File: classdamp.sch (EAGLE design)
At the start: 40 parts, among them IC1 78L05, Q1 BS170, Q10 IRF 9Z34N, Q2 BS170, Q7 IRF 530N, Q8 IRF 530N, Q9 IRF 9Z34N

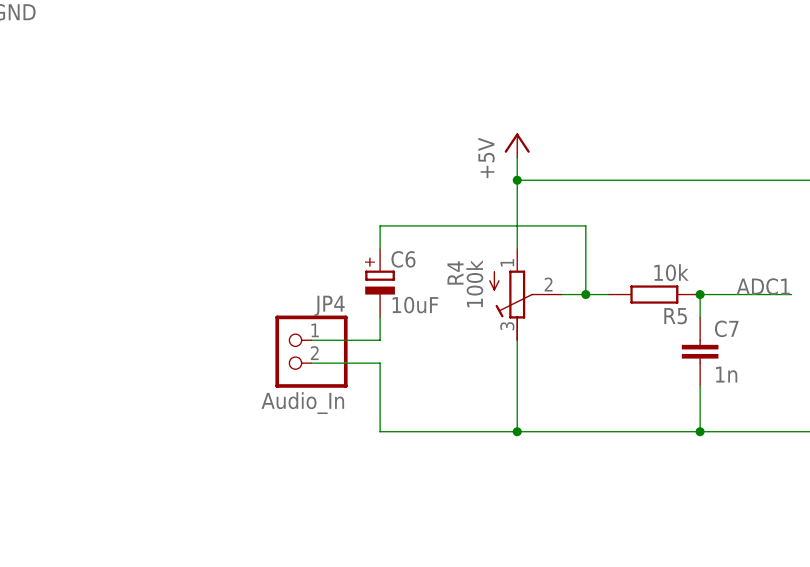
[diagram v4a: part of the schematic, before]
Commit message: updated reichelt order
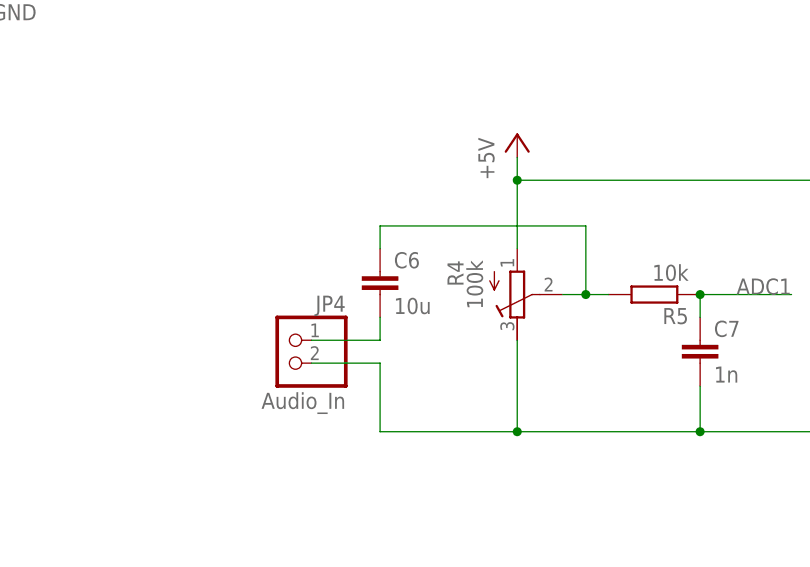
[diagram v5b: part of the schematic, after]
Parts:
- C6: value 10uF -> 10u; device resistor:CPOL-EUE1.8-4 -> resistor:C-EUC0805K
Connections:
- net N$10: now also C6.1; no longer C6.+
- net N$8: now also C6.2; no longer C6.-
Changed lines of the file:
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@@
 <part name="JP6" library="pinhead" deviceset="PINHD-1X3" device="" value="freq_pot"/>
 <part name="JP7" library="pinhead" deviceset="PINHD-1X3" device="" value="vol_pot"/>
-<part name="C6" library="resistor" deviceset="CPOL-EU" device="E1.8-4" value="10uF"/>
 <part name="U$1" library="avr-7" deviceset="TINY26" device="P"/>
 <part name="Q7" library="transistor-power" deviceset="PMOSFET_N" device="TO220BV" value="IRF 530N"/>
@@
 <part name="C7" library="resistor" deviceset="C-EU" device="C0805K" value="1n"/>
 <part name="R5" library="resistor" deviceset="R-EU_" device="R0805" value="10k"/>
+<part name="C6" library="resistor" deviceset="C-EU" device="C0805K" value="10u"/>
 </parts>
 <sheets>
@@
 <instance part="JP6" gate="A" x="91.44" y="0" rot="MR0"/>
 <instance part="JP7" gate="A" x="142.24" y="0" rot="MR0"/>
-<instance part="C6" gate="G$1" x="17.78" y="2.54"/>
 <instance part="U$1" gate="G$1" x="0" y="-60.96"/>
 <instance part="Q7" gate="G$1" x="127" y="45.72"/>
@@
 <instance part="C7" gate="G$1" x="53.34" y="-5.08"/>
 <instance part="R5" gate="G$1" x="48.26" y="0" rot="R180"/>
+<instance part="C6" gate="G$1" x="17.78" y="2.54"/>
 </instances>
 <busses>
@@
 <wire x1="10.16" y1="-5.08" x2="17.78" y2="-5.08" width="0.1524" layer="91"/>
 <wire x1="17.78" y1="-5.08" x2="17.78" y2="-2.54" width="0.1524" layer="91"/>
-<pinref part="C6" gate="G$1" pin="-"/>
+<pinref part="C6" gate="G$1" pin="2"/>
 </segment>
 </net>
 <net name="N$10" class="0">
 <segment>
-<pinref part="C6" gate="G$1" pin="+"/>
 <wire x1="17.78" y1="5.08" x2="17.78" y2="7.62" width="0.1524" layer="91"/>
 <wire x1="17.78" y1="7.62" x2="40.64" y2="7.62" width="0.1524" layer="91"/>
@@
 <junction x="40.64" y="0"/>
 <pinref part="R5" gate="G$1" pin="2"/>
-</segment>
-</net>
+<pinref part="C6" gate="G$1" pin="1"/>
+</segment>
+</net>

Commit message: changed to dual-layer design
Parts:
- added LED2: (no value), led:LEDSML0805
- added R6: 1k, resistor:R-EU_R0805
- D1, D2: device diode:ZENER-DIODEZD-12.5 -> diode:ZENER-DIODEZD-5
- LED1: device led:LED5MM -> led:LEDSML0805
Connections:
- new net N$14: R6.2, U$1.(ADC7/XTAL1)PB4
- new net N$3: LED2.A, R6.1
- net GND: now also LED2.C
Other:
- moved on the sheet: JP8
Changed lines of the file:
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@@
 <grid distance="0.1" unitdist="inch" unit="inch" style="lines" multiple="1" display="no" altdistance="0.01" altunitdist="inch" altunit="inch"/>
 <layers>
-<layer number="1" name="Top" color="4" fill="1" visible="no" active="no"/>
-<layer number="16" name="Bottom" color="1" fill="1" visible="no" active="no"/>
-<layer number="17" name="Pads" color="2" fill="1" visible="no" active="no"/>
-<layer number="18" name="Vias" color="2" fill="1" visible="no" active="no"/>
-<layer number="19" name="Unrouted" color="6" fill="1" visible="no" active="no"/>
-<layer number="20" name="Dimension" color="15" fill="1" visible="no" active="no"/>
-<layer number="21" name="tPlace" color="7" fill="1" visible="no" active="no"/>
-<layer number="22" name="bPlace" color="7" fill="1" visible="no" active="no"/>
-<layer number="23" name="tOrigins" color="15" fill="1" visible="no" active="no"/>
-<layer number="24" name="bOrigins" color="15" fill="1" visible="no" active="no"/>
-<layer number="25" name="tNames" color="7" fill="1" visible="no" active="no"/>
-<layer number="26" name="bNames" color="7" fill="1" visible="no" active="no"/>
-<layer number="27" name="tValues" color="7" fill="1" visible="no" active="no"/>
-<layer number="28" name="bValues" color="7" fill="1" visible="no" active="no"/>
+<layer number="1" name="Top" color="4" fill="1" visible="yes" active="no"/>
+<layer number="16" name="Bottom" color="1" fill="1" visible="yes" active="no"/>
+<layer number="17" name="Pads" color="2" fill="1" visible="yes" active="no"/>
+<layer number="18" name="Vias" color="2" fill="1" visible="yes" active="no"/>
+<layer number="19" name="Unrouted" color="6" fill="1" visible="yes" active="no"/>
+<layer number="20" name="Dimension" color="15" fill="1" visible="yes" active="no"/>
+<layer number="21" name="tPlace" color="7" fill="1" visible="yes" active="no"/>
+<layer number="22" name="bPlace" color="7" fill="1" visible="yes" active="no"/>
+<layer number="23" name="tOrigins" color="15" fill="1" visible="yes" active="no"/>
+<layer number="24" name="bOrigins" color="15" fill="1" visible="yes" active="no"/>
+<layer number="25" name="tNames" color="7" fill="1" visible="yes" active="no"/>
+<layer number="26" name="bNames" color="7" fill="1" visible="yes" active="no"/>
+<layer number="27" name="tValues" color="7" fill="1" visible="yes" active="no"/>
+<layer number="28" name="bValues" color="7" fill="1" visible="yes" active="no"/>
 <layer number="29" name="tStop" color="7" fill="3" visible="no" active="no"/>
 <layer number="30" name="bStop" color="7" fill="6" visible="no" active="no"/>
@@
 <layer number="35" name="tGlue" color="7" fill="4" visible="no" active="no"/>
 <layer number="36" name="bGlue" color="7" fill="5" visible="no" active="no"/>
-<layer number="37" name="tTest" color="7" fill="1" visible="no" active="no"/>
-<layer number="38" name="bTest" color="7" fill="1" visible="no" active="no"/>
+<layer number="37" name="tTest" color="7" fill="1" visible="yes" active="no"/>
+<layer number="38" name="bTest" color="7" fill="1" visible="yes" active="no"/>
 <layer number="39" name="tKeepout" color="4" fill="11" visible="no" active="no"/>
 <layer number="40" name="bKeepout" color="1" fill="11" visible="no" active="no"/>
@@
 <layer number="44" name="Drills" color="7" fill="1" visible="no" active="no"/>
 <layer number="45" name="Holes" color="7" fill="1" visible="no" active="no"/>
-<layer number="46" name="Milling" color="3" fill="1" visible="no" active="no"/>
-<layer number="47" name="Measures" color="7" fill="1" visible="no" active="no"/>
-<layer number="48" name="Document" color="7" fill="1" visible="no" active="no"/>
-<layer number="49" name="Reference" color="7" fill="1" visible="no" active="no"/>
-<layer number="50" name="dxf" color="7" fill="1" visible="no" active="no"/>
-<layer number="51" name="tDocu" color="7" fill="1" visible="no" active="no"/>
-<layer number="52" name="bDocu" color="7" fill="1" visible="no" active="no"/>
+<layer number="46" name="Milling" color="3" fill="1" visible="yes" active="no"/>
+<layer number="47" name="Measures" color="7" fill="1" visible="yes" active="no"/>
+<layer number="48" name="Document" color="7" fill="1" visible="yes" active="no"/>
+<layer number="49" name="Reference" color="7" fill="1" visible="yes" active="no"/>
+<layer number="50" name="dxf" color="7" fill="1" visible="yes" active="no"/>
+<layer number="51" name="tDocu" color="7" fill="1" visible="yes" active="no"/>
+<layer number="52" name="bDocu" color="7" fill="1" visible="yes" active="no"/>
 <layer number="91" name="Nets" color="2" fill="1" visible="yes" active="yes"/>
 <layer number="92" name="Busses" color="1" fill="1" visible="yes" active="yes"/>
@@
 <parts>
 <part name="IC1" library="v-reg" deviceset="78LXX" device="" value="78L05"/>
-<part name="D1" library="diode" deviceset="ZENER-DIODE" device="ZD-12.5" value="6.3V"/>
+<part name="D1" library="diode" deviceset="ZENER-DIODE" device="ZD-5" value="6.3V"/>
 <part name="Q1" library="transistor-small-signal" deviceset="BS170" device=""/>
 <part name="R1" library="resistor" deviceset="R-EU_" device="R0805" value="1k"/>
-<part name="D2" library="diode" deviceset="ZENER-DIODE" device="ZD-12.5" value="6.3V"/>
+<part name="D2" library="diode" deviceset="ZENER-DIODE" device="ZD-5" value="6.3V"/>
 <part name="Q2" library="transistor-small-signal" deviceset="BS170" device=""/>
 <part name="R2" library="resistor" deviceset="R-EU_" device="R0805" value="1k"/>
 <part name="JP4" library="pinhead" deviceset="PINHD-1X2" device="" value="Audio_In"/>
 <part name="C5" library="resistor" deviceset="CPOL-EU" device="E5-8.5" value="1000uF"/>
-<part name="LED1" library="led" deviceset="LED" device="5MM"/>
+<part name="LED1" library="led" deviceset="LED" device="SML0805"/>
 <part name="R4" library="resistor" deviceset="R-TRIMM" device="64W" value="100k"/>
 <part name="JP6" library="pinhead" deviceset="PINHD-1X3" device="" value="freq_pot"/>
@@
 <part name="R5" library="resistor" deviceset="R-EU_" device="R0805" value="10k"/>
 <part name="C6" library="resistor" deviceset="C-EU" device="C0805K" value="10u"/>
+<part name="LED2" library="led" deviceset="LED" device="SML0805"/>
+<part name="R6" library="resistor" deviceset="R-EU_" device="R0805" value="1k"/>
+<part name="GND8" library="supply1" deviceset="GND" device=""/>
 </parts>
 <sheets>
@@
 <instance part="H1" gate="G$1" x="172.72" y="-48.26"/>
 <instance part="JP2" gate="A" x="53.34" y="-43.18" rot="MR0"/>
-<instance part="JP8" gate="A" x="63.5" y="-55.88" rot="MR0"/>
-<instance part="P+5" gate="1" x="83.82" y="-53.34"/>
-<instance part="GND6" gate="1" x="76.2" y="-63.5"/>
+<instance part="JP8" gate="A" x="63.5" y="-60.96" rot="MR0"/>
+<instance part="P+5" gate="1" x="83.82" y="-58.42"/>
+<instance part="GND6" gate="1" x="76.2" y="-68.58"/>
 <instance part="JP1" gate="G$1" x="116.84" y="-68.58" rot="MR0"/>
 <instance part="GND7" gate="1" x="134.62" y="-73.66"/>
@@
 <instance part="R5" gate="G$1" x="48.26" y="0" rot="R180"/>
 <instance part="C6" gate="G$1" x="17.78" y="2.54"/>
+<instance part="LED2" gate="G$1" x="93.98" y="-66.04"/>
+<instance part="R6" gate="G$1" x="93.98" y="-58.42" rot="R90"/>
+<instance part="GND8" gate="1" x="93.98" y="-73.66"/>
 </instances>
 <busses>
@@
 <pinref part="JP8" gate="A" pin="3"/>
 <pinref part="P+5" gate="1" pin="+5V"/>
-<wire x1="66.04" y1="-58.42" x2="83.82" y2="-58.42" width="0.1524" layer="91"/>
-<wire x1="83.82" y1="-58.42" x2="83.82" y2="-55.88" width="0.1524" layer="91"/>
+<wire x1="66.04" y1="-63.5" x2="83.82" y2="-63.5" width="0.1524" layer="91"/>
+<wire x1="83.82" y1="-63.5" x2="83.82" y2="-60.96" width="0.1524" layer="91"/>
 </segment>
 </net>
@@
 <pinref part="JP8" gate="A" pin="2"/>
 <pinref part="GND6" gate="1" pin="GND"/>
-<wire x1="66.04" y1="-55.88" x2="76.2" y2="-55.88" width="0.1524" layer="91"/>
-<wire x1="76.2" y1="-55.88" x2="76.2" y2="-60.96" width="0.1524" layer="91"/>
+<wire x1="66.04" y1="-60.96" x2="76.2" y2="-60.96" width="0.1524" layer="91"/>
+<wire x1="76.2" y1="-60.96" x2="76.2" y2="-66.04" width="0.1524" layer="91"/>
+</segment>
+<segment>
+<pinref part="GND8" gate="1" pin="GND"/>
+<pinref part="LED2" gate="G$1" pin="C"/>
 </segment>
 </net>
@@
 <segment>
 <pinref part="JP8" gate="A" pin="1"/>
-<wire x1="58.42" y1="-53.34" x2="66.04" y2="-53.34" width="0.1524" layer="91"/>
 <pinref part="U$1" gate="G$1" pin="(ADC10/_RESET_)PB7"/>
-<wire x1="22.86" y1="-58.42" x2="58.42" y2="-58.42" width="0.1524" layer="91"/>
-<wire x1="58.42" y1="-58.42" x2="58.42" y2="-53.34" width="0.1524" layer="91"/>
+<wire x1="22.86" y1="-58.42" x2="66.04" y2="-58.42" width="0.1524" layer="91"/>
 </segment>
 </net>
@@
 </segment>
 </net>
+<net name="N$14" class="0">
+<segment>
+<pinref part="U$1" gate="G$1" pin="(ADC7/XTAL1)PB4"/>
+<wire x1="22.86" y1="-50.8" x2="93.98" y2="-50.8" width="0.1524" layer="91"/>
+<pinref part="R6" gate="G$1" pin="2"/>
+<wire x1="93.98" y1="-50.8" x2="93.98" y2="-53.34" width="0.1524" layer="91"/>
+</segment>
+</net>
+<net name="N$3" class="0">
+<segment>
+<pinref part="LED2" gate="G$1" pin="A"/>
+<pinref part="R6" gate="G$1" pin="1"/>
+</segment>
+</net>
